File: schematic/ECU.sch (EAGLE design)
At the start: 29 parts, among them J1 Break, J2 COMM, J3 PWR, J4 DISPLAY, J5 THROTTLE, J6 LED, J7 SPEED, Q1 NMOSFET, Q2 NMOSFET, Q4 BSS84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

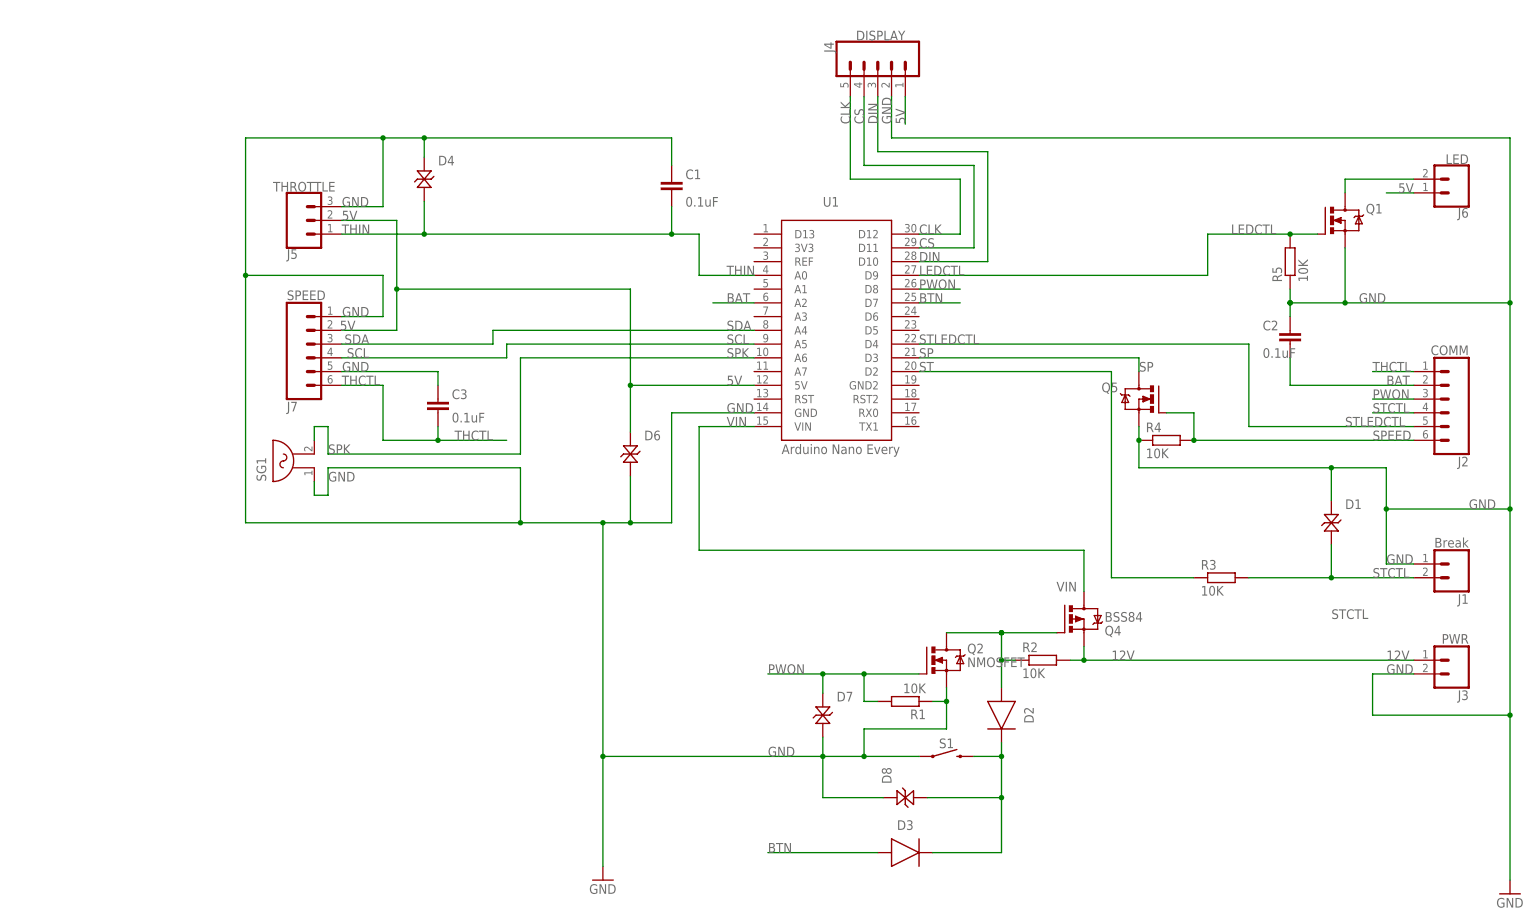
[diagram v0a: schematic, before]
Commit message: Prettify ECU schematic according to #1
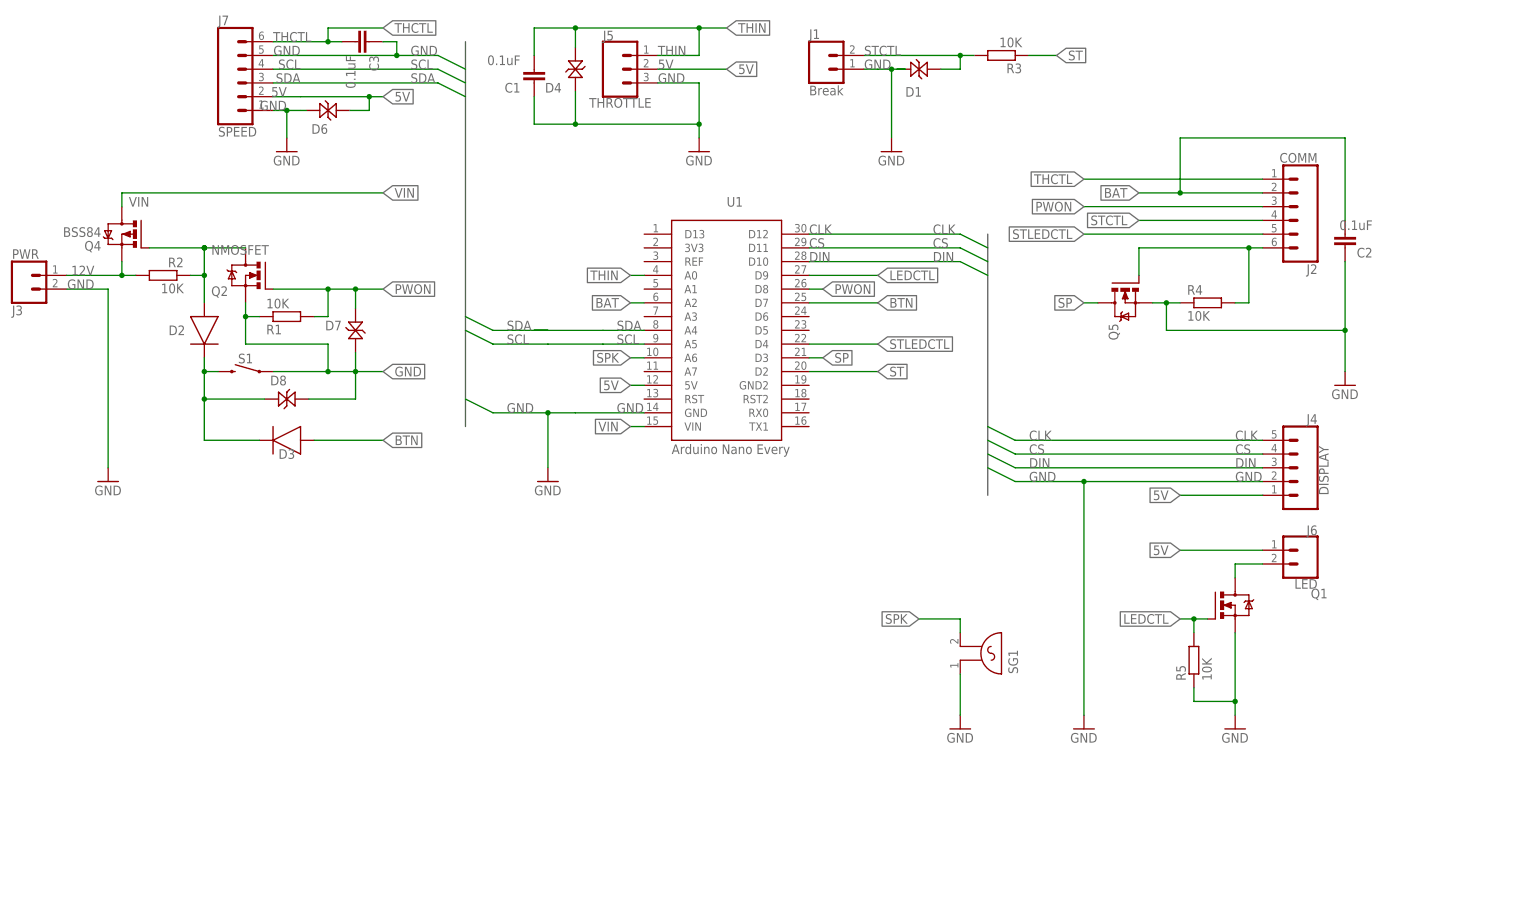
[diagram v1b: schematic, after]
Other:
- moved on the sheet: C1, C2, C3, D1, D2, D3, D4, D6, D7, D8, J1, J2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
